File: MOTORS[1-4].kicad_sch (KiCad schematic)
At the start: 5 parts, among them U4 ZX-SH1.0-8PWT

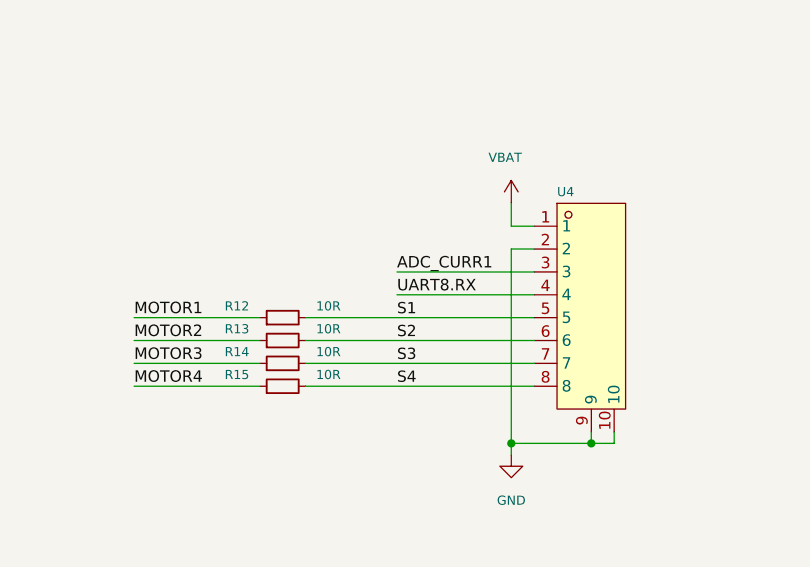
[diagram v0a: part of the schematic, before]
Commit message: grouped ICs and passives
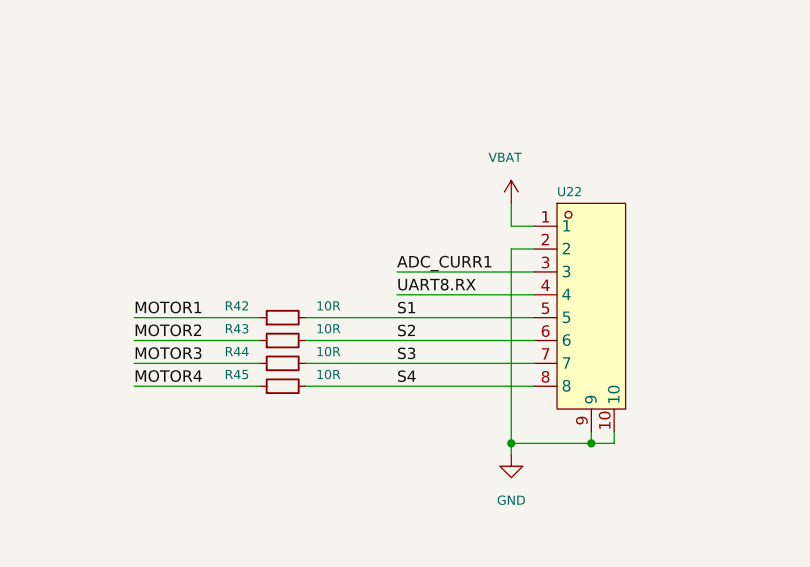
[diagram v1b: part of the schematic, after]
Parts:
- renumbered R12 to R42, R13 to R43, R14 to R44, R15 to R45, U4 to U22
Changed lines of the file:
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@@
 		(dnp no)
 		(fields_autoplaced yes)
-		(property "Reference" "#PWR027"
+		(property "Reference" "#PWR0119"
 			(at 114.3 82.55 0)
 			(hide yes)
@@
 			(project "LEVIA_H7"
 				(path "/6b768b36-fce6-4be0-9021-6d41bddc3a70/647d5d7a-ea7f-42b5-bbeb-8045c387a5e2"
-					(reference "#PWR027")
+					(reference "#PWR0119")
 					(unit 1)
 				)
@@
 		(in_pos_files yes)
 		(dnp no)
-		(property "Reference" "R12"
+		(property "Reference" "R42"
 			(at 83.82 59.69 90)
 			(show_name no)
@@
 			(project "LEVIA_H7"
 				(path "/6b768b36-fce6-4be0-9021-6d41bddc3a70/647d5d7a-ea7f-42b5-bbeb-8045c387a5e2"
-					(reference "R12")
+					(reference "R42")
 					(unit 1)
 				)
@@
 		(in_pos_files yes)
 		(dnp no)
-		(property "Reference" "R14"
+		(property "Reference" "R44"
 			(at 83.82 64.77 90)
 			(show_name no)
@@
 			(project "LEVIA_H7"
 				(path "/6b768b36-fce6-4be0-9021-6d41bddc3a70/647d5d7a-ea7f-42b5-bbeb-8045c387a5e2"
-					(reference "R14")
+					(reference "R44")
 					(unit 1)
 				)
@@
 		(in_pos_files yes)
 		(dnp no)
-		(property "Reference" "R15"
+		(property "Reference" "R45"
 			(at 83.82 67.31 90)
 			(show_name no)
@@
 			(project "LEVIA_H7"
 				(path "/6b768b36-fce6-4be0-9021-6d41bddc3a70/647d5d7a-ea7f-42b5-bbeb-8045c387a5e2"
-					(reference "R15")
+					(reference "R45")
 					(unit 1)
 				)
@@
 		(in_pos_files yes)
 		(dnp no)
-		(property "Reference" "#PWR089"
+		(property "Reference" "#PWR0118"
 			(at 114.3 52.07 0)
 			(hide yes)
@@
 			(project "LEVIA_H7"
 				(path "/6b768b36-fce6-4be0-9021-6d41bddc3a70/647d5d7a-ea7f-42b5-bbeb-8045c387a5e2"
-					(reference "#PWR089")
+					(reference "#PWR0118")
 					(unit 1)
 				)
@@
 		(in_pos_files yes)
 		(dnp no)
-		(property "Reference" "R13"
+		(property "Reference" "R43"
 			(at 83.82 62.23 90)
 			(show_name no)
@@
 			(project "LEVIA_H7"
 				(path "/6b768b36-fce6-4be0-9021-6d41bddc3a70/647d5d7a-ea7f-42b5-bbeb-8045c387a5e2"
-					(reference "R13")
+					(reference "R43")
 					(unit 1)
 				)
@@
 		(in_pos_files yes)
 		(dnp no)
-		(property "Reference" "U4"
+		(property "Reference" "U22"
 			(at 119.38 46.99 0)
 			(show_name no)
@@
 			(project "LEVIA_H7"
 				(path "/6b768b36-fce6-4be0-9021-6d41bddc3a70/647d5d7a-ea7f-42b5-bbeb-8045c387a5e2"
-					(reference "U4")
-					(unit 1)
-				)
+					(reference "U22")
+					(unit 1)
+				)
